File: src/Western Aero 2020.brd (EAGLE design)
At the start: 118.7 x 105.4 mm, 97 parts, among them IC1 LT1963AET, IC2 LT1963AET, J1 PITOT, J10 ANA_IO, J11 PWR, J2 BUZZER, J3 RX2/TX2, J4 RX3/TX3, J5 SPI, J6 DIG_IO, J7 RX1/TX1, J8 DIG_IO, J9 REF/GND, U3 TEENSY_3.5_DIL+4, U5 SPARKFUN_MPU9250_IMU, U6 ADAFRUIT_MPL3115A2_BAROMETER, U7 ADAFRUIT_INA219_BATTERY_SENSOR, U8 ADAFRUIT_RFM95W_LORA_RADIO, U9 ADAFRUIT_MTK3339_GPS

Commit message: Trace rework
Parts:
- J8: device SparkFun-Connectors:1X04 -> SparkFun-Connectors:1X05
- moved J8 0.71 mm to (96.5, 63.5)
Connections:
- removed net CS: J5.4, U3.33/A14, U8.8
- new net D33: J8.5, U3.33/A14
- new net TX_2: J5.4, U8.8
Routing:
- net D33: track 0.00 -> 77.0 mm, vias 0 -> 1
- net CS: track 49.1 -> 0.00 mm
- net TX_2: track 0.00 -> 35.7 mm
- net GPS_PPS: track 29.2 -> 28.5 mm
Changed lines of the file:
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@@
 <attribute name="VALUE" x="112.932" y="27.08" size="0.6096" layer="27" font="vector" ratio="20" rot="R90"/>
-</element>
-<element name="J8" library="SparkFun-Connectors" library_urn="urn:adsk.eagle:library:513" package="1X04" package3d_urn="urn:adsk.eagle:package:38085/1" value="DIG_IO" x="97" y="64" smashed="yes" rot="R180">
-<attribute name="PROD_ID" value="CONN-09696" x="97" y="64" size="1.778" layer="27" rot="R180" display="off"/>
-<attribute name="VALUE" x="98.27" y="66.032" size="0.6096" layer="27" font="vector" ratio="20" rot="R180"/>
 </element>
 <element name="R1" library="SparkFun-Resistors" library_urn="urn:adsk.eagle:library:532" package="AXIAL-0.3" package3d_urn="urn:adsk.eagle:package:39658/1" value="220" x="84.95" y="33.6" smashed="yes" rot="R90">
@@
 <attribute name="PROD_ID" value="RES-8371" x="45.5" y="16" size="1.778" layer="27" display="off"/>
 <attribute name="VALUE" x="45.5" y="14.984" size="0.6096" layer="27" font="vector" ratio="20" align="top-center"/>
+</element>
+<element name="J8" library="SparkFun-Connectors" library_urn="urn:adsk.eagle:library:513" package="1X05" package3d_urn="urn:adsk.eagle:package:38104/1" value="DIG_IO" x="96.5" y="63.5" smashed="yes" rot="R180">
+<attribute name="NAME" x="97.77" y="62.103" size="0.6096" layer="25" font="vector" ratio="20" rot="R180"/>
+<attribute name="VALUE" x="97.77" y="65.532" size="0.6096" layer="27" font="vector" ratio="20" rot="R180"/>
 </element>
 </elements>
@@
 <wire x1="53" y1="26.54" x2="48.42" y2="31.12" width="0.2032" layer="1"/>
 </signal>
-<signal name="CS">
-<contactref element="U8" pad="8"/>
-<contactref element="U3" pad="33/A14"/>
-<contactref element="J5" pad="4"/>
-<wire x1="46.21" y1="31.45" x2="49.18" y2="34.42" width="0.2032" layer="1"/>
-<wire x1="49.18" y1="34.42" x2="49.18" y2="43.31" width="0.2032" layer="1"/>
-<wire x1="45.88" y1="31.12" x2="46.21" y2="31.45" width="0.2032" layer="1"/>
-<wire x1="34.5" y1="14.12" x2="50.12" y2="14.12" width="0.2032" layer="1"/>
-<wire x1="50.12" y1="14.12" x2="51.5" y2="15.5" width="0.2032" layer="1"/>
-<wire x1="51.5" y1="15.5" x2="51.5" y2="23" width="0.2032" layer="1"/>
-<wire x1="45.88" y1="28.62" x2="45.88" y2="31.12" width="0.2032" layer="1"/>
-<wire x1="51.5" y1="23" x2="45.88" y2="28.62" width="0.2032" layer="1"/>
-</signal>
 <signal name="LORA_RST">
 <contactref element="U8" pad="9"/>
@@
 <contactref element="U9" pad="RX"/>
 <wire x1="89.055" y1="56.775" x2="87.28" y2="58.55" width="0.2032" layer="16"/>
-<wire x1="80.54" y1="77.26" x2="87.28" y2="70.52" width="0.2032" layer="16"/>
-<wire x1="87.28" y1="70.52" x2="87.28" y2="58.55" width="0.2032" layer="16"/>
 <wire x1="111.5" y1="64.62" x2="106.325" y2="59.445" width="0.2032" layer="16"/>
 <wire x1="106.325" y1="59.445" x2="106.325" y2="58.05" width="0.2032" layer="16"/>
 <wire x1="106.325" y1="58.05" x2="105.05" y2="56.775" width="0.2032" layer="16"/>
 <wire x1="105.05" y1="56.775" x2="89.055" y2="56.775" width="0.2032" layer="16"/>
+<wire x1="87.28" y1="58.55" x2="82.5" y2="63.33" width="0.2032" layer="16"/>
+<wire x1="82.5" y1="75.3" x2="80.54" y2="77.26" width="0.2032" layer="16"/>
+<wire x1="82.5" y1="63.33" x2="82.5" y2="75.3" width="0.2032" layer="16"/>
 </signal>
 <signal name="TX3">
@@
 <contactref element="U3" pad="16/A2"/>
 <wire x1="80.54" y1="82.34" x2="79" y2="80.8" width="0.2032" layer="16"/>
-<wire x1="79" y1="80.8" x2="79" y2="66" width="0.2032" layer="16"/>
-<wire x1="80.925" y1="64.075" x2="79" y2="66" width="0.2032" layer="16"/>
+<wire x1="79" y1="80.8" x2="79" y2="61" width="0.2032" layer="16"/>
+<wire x1="80.925" y1="59.075" x2="79" y2="61" width="0.2032" layer="16"/>
 <wire x1="82.2" y1="43.31" x2="80.925" y2="44.585" width="0.2032" layer="16"/>
-<wire x1="80.925" y1="44.585" x2="80.925" y2="64.075" width="0.2032" layer="16"/>
+<wire x1="80.925" y1="44.585" x2="80.925" y2="59.075" width="0.2032" layer="16"/>
 </signal>
 <signal name="GPS_PPS">
 <contactref element="U9" pad="PPS"/>
 <contactref element="U3" pad="17/A3"/>
-<wire x1="80.54" y1="69.64" x2="82.36" y2="69.64" width="0.2032" layer="16"/>
-<wire x1="82.36" y1="69.64" x2="83.5" y2="68.5" width="0.2032" layer="16"/>
-<wire x1="83.5" y1="68.5" x2="83.5" y2="57.4" width="0.2032" layer="16"/>
-<wire x1="83.5" y1="57.4" x2="83.475" y2="57.375" width="0.2032" layer="16"/>
-<wire x1="83.475" y1="57.375" x2="83.475" y2="44.575" width="0.2032" layer="16"/>
-<wire x1="83.475" y1="44.575" x2="84.74" y2="43.31" width="0.2032" layer="16"/>
+<wire x1="80.54" y1="69.64" x2="80.54" y2="61.46" width="0.2032" layer="16"/>
+<wire x1="82.325" y1="59.675" x2="83.1" y2="59.675" width="0.2032" layer="16"/>
+<wire x1="83.1" y1="59.675" x2="83.475" y2="59.3" width="0.2032" layer="16"/>
+<wire x1="84.74" y1="54.26" x2="84.74" y2="43.31" width="0.2032" layer="16"/>
+<wire x1="80.54" y1="61.46" x2="82.325" y2="59.675" width="0.2032" layer="16"/>
+<wire x1="83.475" y1="59.3" x2="83.475" y2="55.525" width="0.2032" layer="16"/>
+<wire x1="83.475" y1="55.525" x2="84.74" y2="54.26" width="0.2032" layer="16"/>
 </signal>
 <signal name="VUSB">
@@
 </signal>
 <signal name="D3">
-<contactref element="J8" pad="1"/>
 <contactref element="U3" pad="3"/>
 <contactref element="U7" pad="ALERT"/>
-<wire x1="97" y1="64" x2="97" y2="58.99" width="0.2032" layer="16"/>
 <wire x1="97" y1="58.99" x2="97.44" y2="58.55" width="0.2032" layer="16"/>
 <via x="58.5" y="53" extent="1-16" drill="0.508"/>
 <wire x1="58.5" y1="53" x2="62" y2="56.5" width="0.2032" layer="1"/>
 <wire x1="95.39" y1="56.5" x2="97.44" y2="58.55" width="0.2032" layer="1"/>
-<wire x1="58.5" y1="53" x2="46" y2="53" width="0.2032" layer="16"/>
-<wire x1="46" y1="53" x2="45.85" y2="53" width="0.2032" layer="16"/>
+<wire x1="58.5" y1="53" x2="44.85" y2="53" width="0.2032" layer="16"/>
 <wire x1="62" y1="56.5" x2="95.39" y2="56.5" width="0.2032" layer="1"/>
-<wire x1="45.85" y1="53" x2="44.85" y2="53" width="0.2032" layer="16"/>
 <wire x1="44.85" y1="53" x2="44.2" y2="52.35" width="0.2032" layer="16"/>
+<contactref element="J8" pad="1"/>
+<wire x1="96.5" y1="63.5" x2="97" y2="63" width="0.2032" layer="16"/>
+<wire x1="97" y1="63" x2="97" y2="58.99" width="0.2032" layer="16"/>
 </signal>
 <signal name="D4">
+<contactref element="U3" pad="4"/>
 <contactref element="J8" pad="2"/>
-<contactref element="U3" pad="4"/>
-<wire x1="94.46" y1="64" x2="94.46" y2="58.99" width="0.2032" layer="16"/>
-<wire x1="94.46" y1="58.99" x2="94.9" y2="58.55" width="0.2032" layer="16"/>
+<wire x1="94.9" y1="58.55" x2="93.96" y2="59.49" width="0.2032" layer="16"/>
+<wire x1="93.96" y1="59.49" x2="93.96" y2="63.5" width="0.2032" layer="16"/>
 </signal>
 <signal name="D5">
+<contactref element="U3" pad="5"/>
 <contactref element="J8" pad="3"/>
-<contactref element="U3" pad="5"/>
-<wire x1="91.92" y1="64" x2="91.92" y2="58.99" width="0.2032" layer="16"/>
-<wire x1="91.92" y1="58.99" x2="92.36" y2="58.55" width="0.2032" layer="16"/>
+<wire x1="92.36" y1="58.55" x2="91.42" y2="59.49" width="0.2032" layer="16"/>
+<wire x1="91.42" y1="59.49" x2="91.42" y2="63.5" width="0.2032" layer="16"/>
 </signal>
 <signal name="D6">
+<contactref element="U3" pad="6"/>
 <contactref element="J8" pad="4"/>
-<contactref element="U3" pad="6"/>
-<wire x1="89.38" y1="64" x2="89.38" y2="58.99" width="0.2032" layer="16"/>
-<wire x1="89.38" y1="58.99" x2="89.82" y2="58.55" width="0.2032" layer="16"/>
+<wire x1="89.82" y1="58.55" x2="88.88" y2="59.49" width="0.2032" layer="16"/>
+<wire x1="88.88" y1="59.49" x2="88.88" y2="63.5" width="0.2032" layer="16"/>
 </signal>
 <signal name="N$2">
@@
 <wire x1="9.865" y1="37.365" x2="10" y2="37.5" width="2" layer="1"/>
 </signal>
+<signal name="TX_2">
+<contactref element="U8" pad="8"/>
+<contactref element="J5" pad="4"/>
+<wire x1="34.5" y1="14.12" x2="50.12" y2="14.12" width="0.2032" layer="1"/>
+<wire x1="50.12" y1="14.12" x2="51.5" y2="15.5" width="0.2032" layer="1"/>
+<wire x1="51.5" y1="15.5" x2="51.5" y2="24.5" width="0.2032" layer="1"/>
+<wire x1="46.21" y1="29.79" x2="46.21" y2="31.45" width="0.2032" layer="1"/>
+<wire x1="51.5" y1="24.5" x2="46.21" y2="29.79" width="0.2032" layer="1"/>
+</signal>
+<signal name="D33">
+<contactref element="U3" pad="33/A14"/>
+<contactref element="J8" pad="5"/>
+<wire x1="86.34" y1="63.5" x2="86.34" y2="64.84" width="0.2032" layer="1"/>
+<wire x1="86.34" y1="64.84" x2="87" y2="65.5" width="0.2032" layer="1"/>
+<wire x1="87" y1="65.5" x2="96.5" y2="65.5" width="0.2032" layer="1"/>
+<wire x1="98.775" y1="63.225" x2="98.775" y2="57.475" width="0.2032" layer="1"/>
+<wire x1="98.775" y1="57.475" x2="90.8" y2="49.5" width="0.2032" layer="1"/>
+<wire x1="63.5" y1="49.5" x2="61" y2="47" width="0.2032" layer="1"/>
+<wire x1="61" y1="47" x2="55" y2="47" width="0.2032" layer="1"/>
+<wire x1="55" y1="47" x2="54" y2="48" width="0.2032" layer="1"/>
+<via x="54" y="48" extent="1-16" drill="0.508"/>
+<wire x1="54" y1="48" x2="49.31" y2="43.31" width="0.2032" layer="16"/>
+<wire x1="49.31" y1="43.31" x2="49.18" y2="43.31" width="0.2032" layer="16"/>
+<wire x1="96.5" y1="65.5" x2="98.775" y2="63.225" width="0.2032" layer="1"/>
+<wire x1="90.8" y1="49.5" x2="63.5" y2="49.5" width="0.2032" layer="1"/>
+</signal>
 </signals>

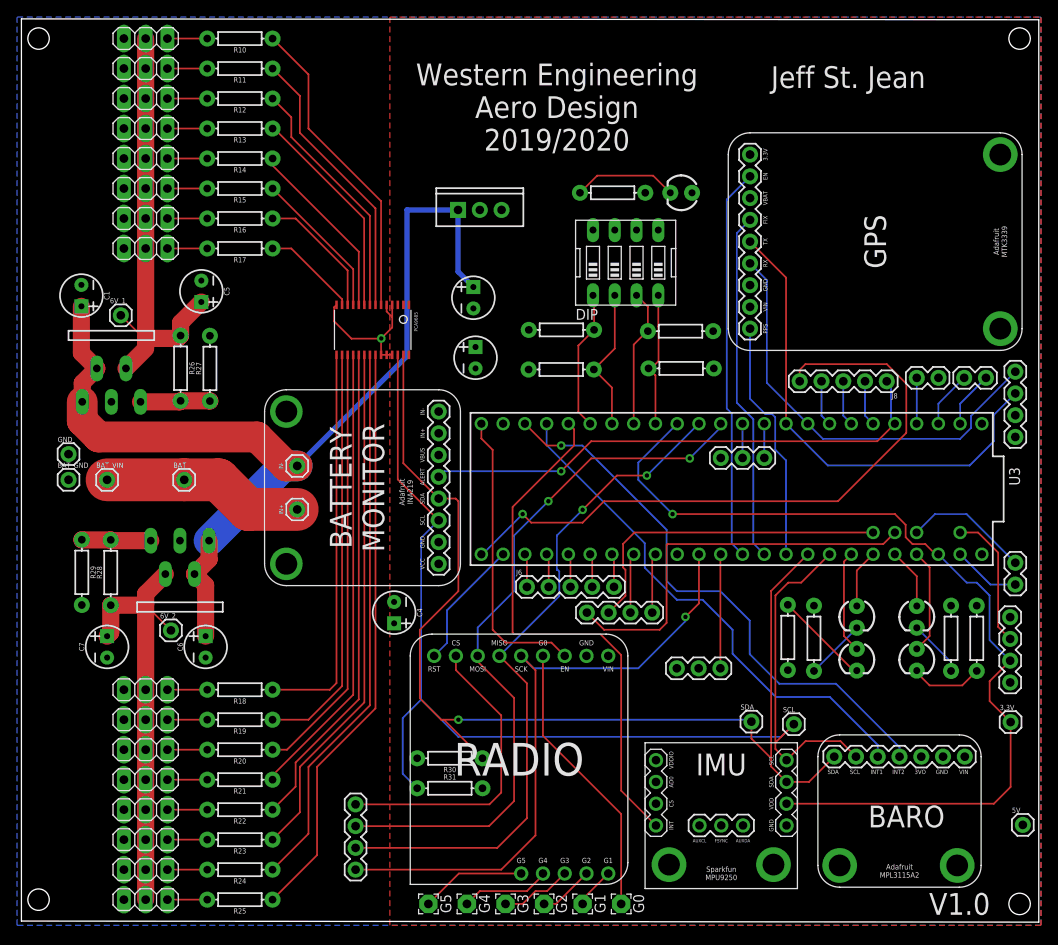
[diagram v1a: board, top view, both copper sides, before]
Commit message: Remove battery monitor
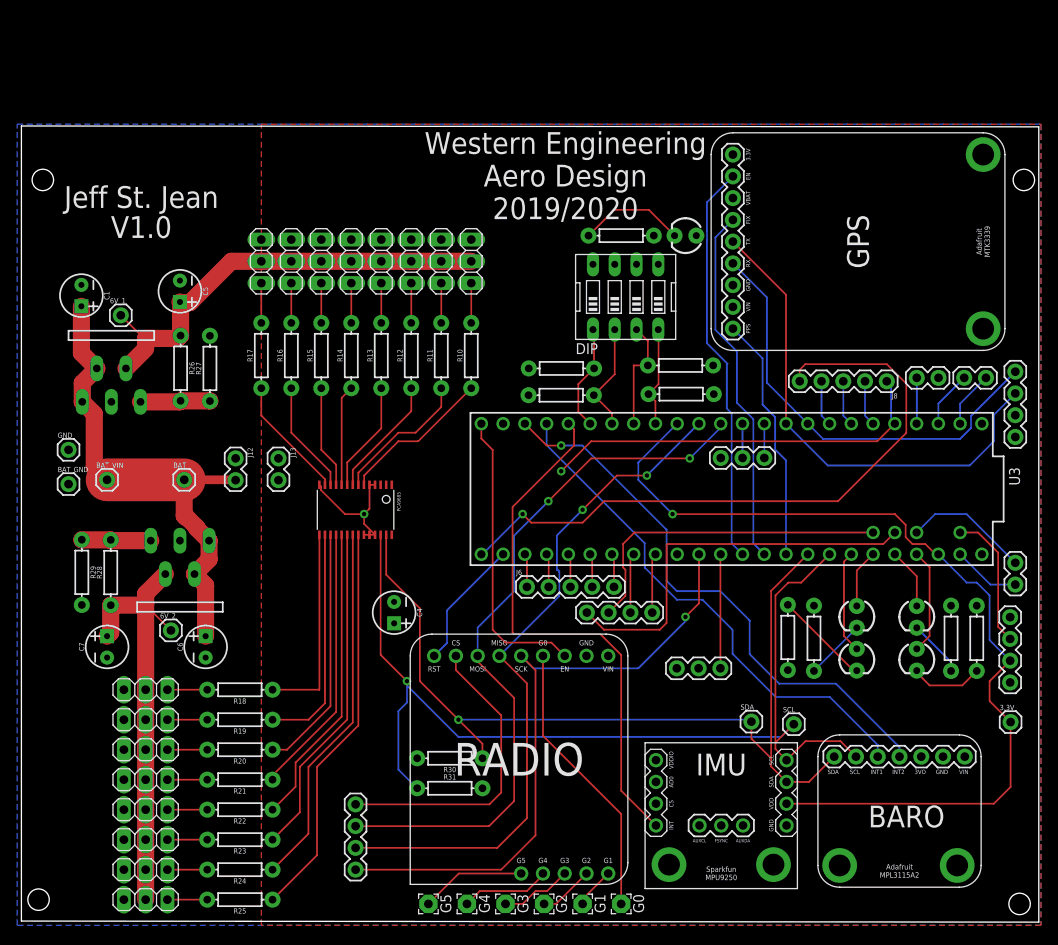
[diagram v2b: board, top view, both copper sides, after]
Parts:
- removed 5V: (no value), SparkFun-Connectors:1X01
- removed 7805: 7805, SparkFun-IC-Power:TO220-IGO
- removed C2: 0.33uF, SparkFun-Capacitors:CPOL-RADIAL-2.5MM-5MM
- removed C3: 0.1uF, SparkFun-Capacitors:CPOL-RADIAL-2.5MM-5MM
- removed U7: ADAFRUIT_INA219_BATTERY_SENSOR, AERO_Eagle_Library:ADAFRUIT_INA219_BATTERY_SENSOR
- added J12: UBEC+, SparkFun-Connectors:1X02
- added J13: UBEC-, SparkFun-Connectors:1X02
- moved JP1 46.0 mm to (48.0, 77.5), turned to 90 degrees
- moved R10 45.8 mm to (48.0, 66.5), turned to 90 degrees
- moved JP2 41.2 mm to (44.5, 77.5), turned to 90 degrees
- moved R11 40.9 mm to (44.5, 66.5), turned to 90 degrees
- moved JP3 36.4 mm to (41.0, 77.5), turned to 90 degrees
- moved R12 36.1 mm to (41.0, 66.5), turned to 90 degrees
- moved JP4 31.6 mm to (37.5, 77.5), turned to 90 degrees
- moved R13 31.2 mm to (37.5, 66.5), turned to 90 degrees
- moved JP5 26.8 mm to (34.0, 77.5), turned to 90 degrees
- moved R14 26.4 mm to (34.0, 66.5), turned to 90 degrees
- moved JP6 22.2 mm to (30.5, 77.5), turned to 90 degrees
- moved R15 21.7 mm to (30.5, 66.5), turned to 90 degrees
- moved PCA9685 21.1 mm to (34.5, 48.5)
- moved JP7 17.7 mm to (27.0, 77.5), turned to 90 degrees
- moved R16 17.1 mm to (27.0, 66.5), turned to 90 degrees
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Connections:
- removed net VIN+: BAT.1, BAT_VIN.1, U7.IN+_TER
- removed net VIN-: 7805.IN, C1.1, C2.1, C6.1, IC1.1, IC1.2, IC2.1, IC2.2, U7.IN-_TER
- new net BAT+: BAT.1, BAT_VIN.1, C1.1, C6.1, IC1.1, IC1.2, IC2.1, IC2.2, J12.2
- net 5V: now also J13.1; no longer 5V.1, 7805.OUT, C3.1, U7.VCC
- net D3: no longer U7.ALERT
- net GND: now also J12.1, J13.2; no longer 7805.GND, C2.2, C3.2, U7.GND
- net SCL: no longer U7.SCL
- net SDA: no longer U7.SDA
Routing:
- net VIN-: track 119.3 -> 0.00 mm
- net BAT+: track 0.00 -> 58.7 mm
- net SDA: track 133.1 -> 106.1 mm
- net VIN+: track 23.6 -> 0.00 mm
- net PWM8: track 46.1 -> 23.5 mm
- net PWM12: track 57.3 -> 35.4 mm
- net PWM11: track 53.5 -> 31.7 mm
- net PWM15: track 68.6 -> 46.7 mm
- net PWM9: track 48.4 -> 26.6 mm
- net PWM14: track 64.8 -> 43.0 mm
- net PWM13: track 61.0 -> 39.2 mm
- net PWM10: track 50.7 -> 28.9 mm
- net SCL: track 141.8 -> 121.8 mm, vias 0 -> 1
- net PWM0: track 36.3 -> 17.8 mm
- net PWM1: track 32.6 -> 16.5 mm
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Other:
- board size 118.7 x 105.4 mm -> 118.7 x 92.9 mm

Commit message: UBEC now supplies 6v with a 5v reg for onboard systems
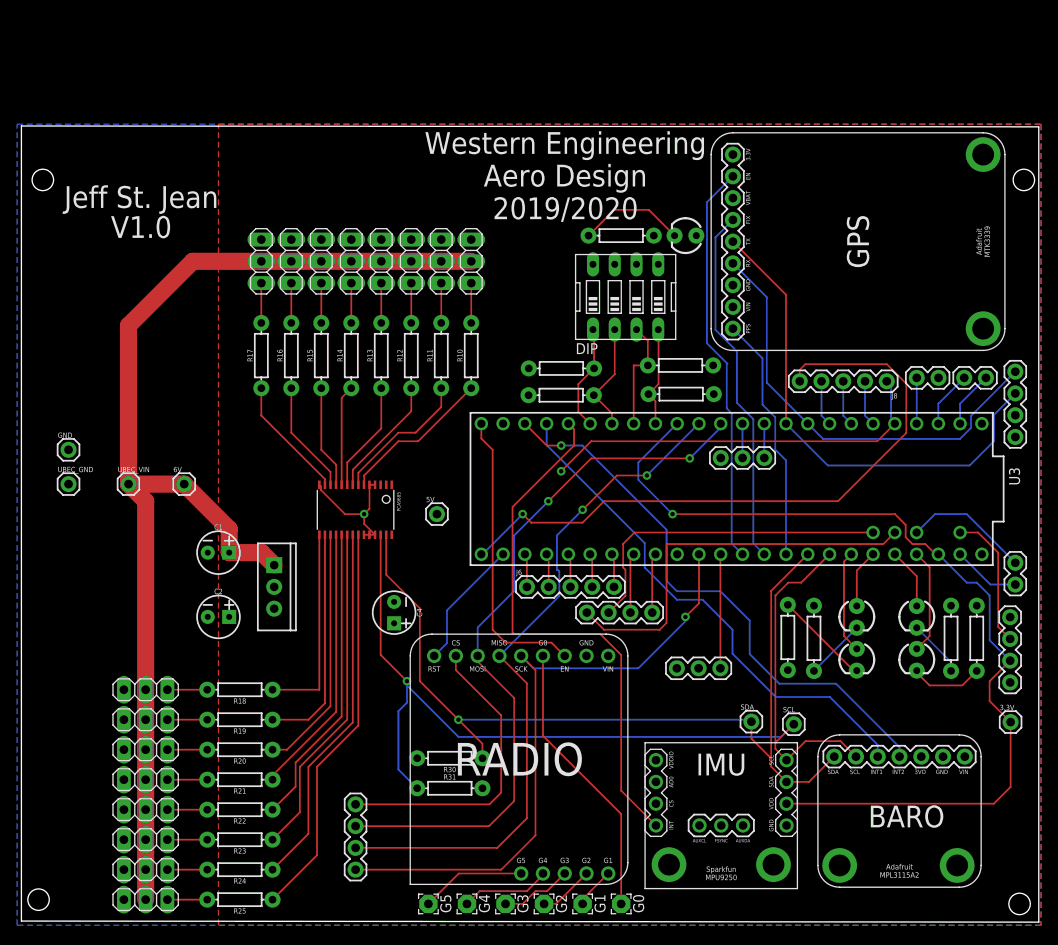
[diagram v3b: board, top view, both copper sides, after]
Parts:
- removed 6V_1, 6V_2, BAT, BAT_VIN: (no value), SparkFun-Connectors:1X01
- removed C5, C7: 22uF, SparkFun-Capacitors:CPOL-RADIAL-2.5MM-5MM
- removed C6: 10uF, SparkFun-Capacitors:CPOL-RADIAL-2.5MM-5MM
- removed IC1, IC2: LT1963AET, linear-technology:TO220-5
- removed J12: UBEC+, SparkFun-Connectors:1X02
- removed J13: UBEC-, SparkFun-Connectors:1X02
- removed R26, R28: 3800, SparkFun-Resistors:AXIAL-0.3
- removed R27, R29: 1000, SparkFun-Resistors:AXIAL-0.3
- added 5V, 6V, UBEC_VIN: (no value), SparkFun-Connectors:1X01
- added C2: 22uF, SparkFun-Capacitors:CPOL-RADIAL-2.5MM-5MM
- added U1: (no value), SparkFun-IC-Power:TO220-IGO
- C1: value 10uF -> 0.47uF
- moved C1 34.0 mm to (18.5, 43.5), turned to 0 degrees
- renumbered BAT_GND to UBEC_GND
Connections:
- removed net 6V_1: 6V_1.1, C5.1, IC2.4, JP1.2, JP2.2, JP3.2, JP4.2, JP5.2, JP6.2, JP7.2, JP8.2, R26.P$1
- removed net 6V_2: 6V_2.1, C7.1, IC1.4, JP10.2, JP11.2, JP12.2, JP13.2, JP14.2, JP15.2, JP16.2, JP9.2, R28.P$1
- removed net BAT+: BAT.1, BAT_VIN.1, C1.1, C6.1, IC1.1, IC1.2, IC2.1, IC2.2, J12.2
- removed net N$28: IC1.5, R28.P$2, R29.P$1
- removed net N$29: IC2.5, R26.P$2, R27.P$1
- new net 6V: 6V.1, C1.1, JP1.2, JP10.2, JP11.2, JP12.2, JP13.2, JP14.2, JP15.2, JP16.2, JP2.2, JP3.2, JP4.2, JP5.2, JP6.2, JP7.2, JP8.2, JP9.2, U1.IN, UBEC_VIN.1
- net 5V: now also 5V.1, C2.1, U1.OUT; no longer J13.1
- net GND: now also C2.2; no longer C5.2, C6.2, C7.2, IC1.3, IC2.3, J12.1, J13.2, R27.P$2, R29.P$2
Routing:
- net 6V: track 0.00 -> 133.5 mm
- net BAT+: track 58.7 -> 0.00 mm
- net 6V_1: track 52.9 -> 0.00 mm
- net 6V_2: track 51.2 -> 0.00 mm
- net N$29: track 8.16 -> 0.00 mm
- net N$28: track 8.10 -> 0.00 mm

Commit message: Reduce board size
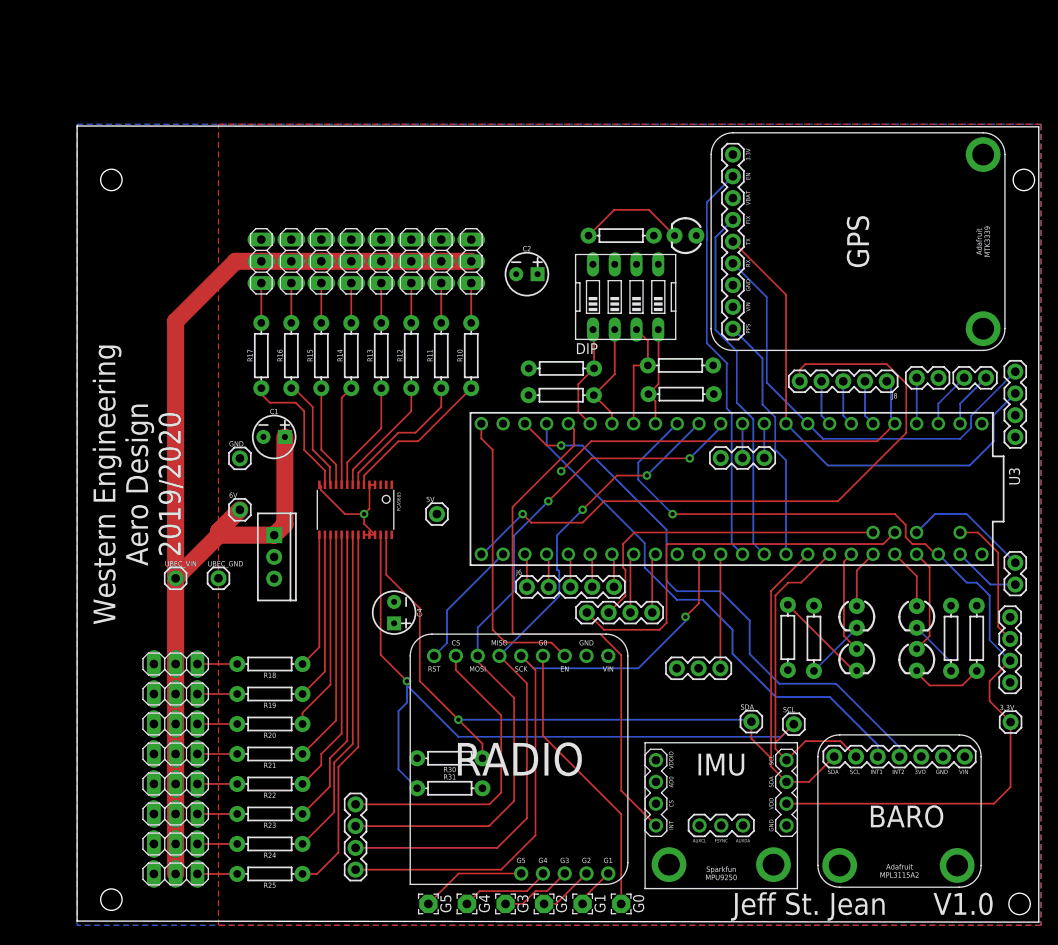
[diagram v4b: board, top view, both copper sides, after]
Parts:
- moved C2 53.8 mm to (54.5, 76.0)
- moved UBEC_GND 20.7 mm to (18.5, 40.5)
- moved GND 20.0 mm to (21.0, 54.5)
- moved C1 15.0 mm to (25.0, 57.0)
- moved UBEC_VIN 12.3 mm to (13.5, 40.5)
- moved 6V 7.16 mm to (21.0, 48.5)
- moved JP10 4.61 mm to (13.5, 27.0)
- moved JP11 4.61 mm to (13.5, 23.5)
- moved JP12 4.61 mm to (13.5, 20.0)
- moved JP13 4.61 mm to (13.5, 16.5)
- moved JP14 4.61 mm to (13.5, 13.0)
- moved JP15 4.61 mm to (13.5, 9.50)
- moved JP16 4.61 mm to (13.5, 6.00)
- moved JP9 4.61 mm to (13.5, 30.5)
- moved R18 4.61 mm to (24.5, 30.5)
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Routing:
- net PWM8: track 23.5 -> 15.9 mm
- net PWM9: track 26.6 -> 19.7 mm
- net PWM10: track 28.9 -> 23.4 mm
- net PWM11: track 31.7 -> 27.2 mm
- net PWM14: track 43.0 -> 38.5 mm
- net PWM13: track 39.2 -> 34.7 mm
- net PWM12: track 35.4 -> 31.0 mm
- net PWM15: track 46.7 -> 43.3 mm
- net 6V: track 133.5 -> 131.4 mm
- net PWM7: track 14.3 -> 16.1 mm
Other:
- board size 118.7 x 92.9 mm -> 112.2 x 92.9 mm
